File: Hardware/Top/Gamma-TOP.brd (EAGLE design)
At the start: 38 x 38 mm, 65 parts, among them SW1 SWITCH.MOM, SW2 SWITCH.MOM, U1 FT231XS, U3 NRF52832_MODULE_MDBT42, U4 PCF8523

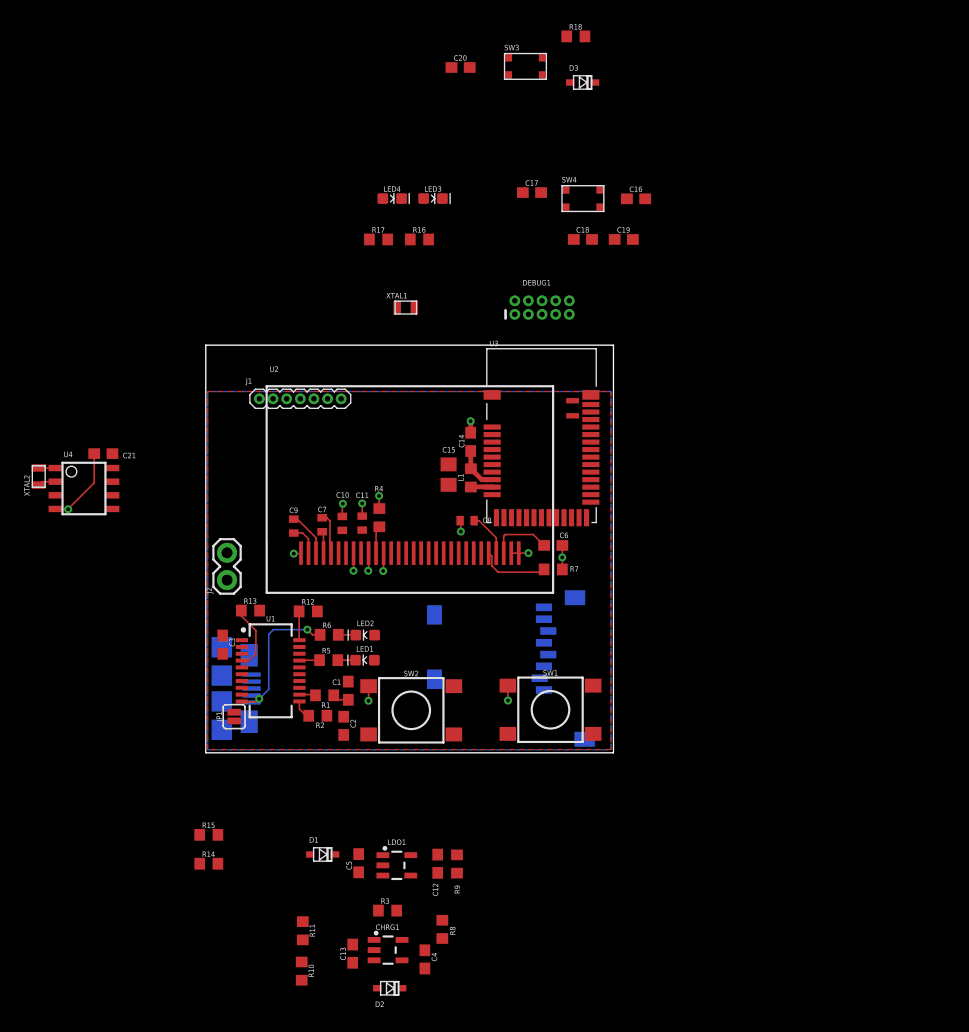
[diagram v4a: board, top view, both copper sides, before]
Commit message: This is the routing as of Take 006 before the removal of the SD Card
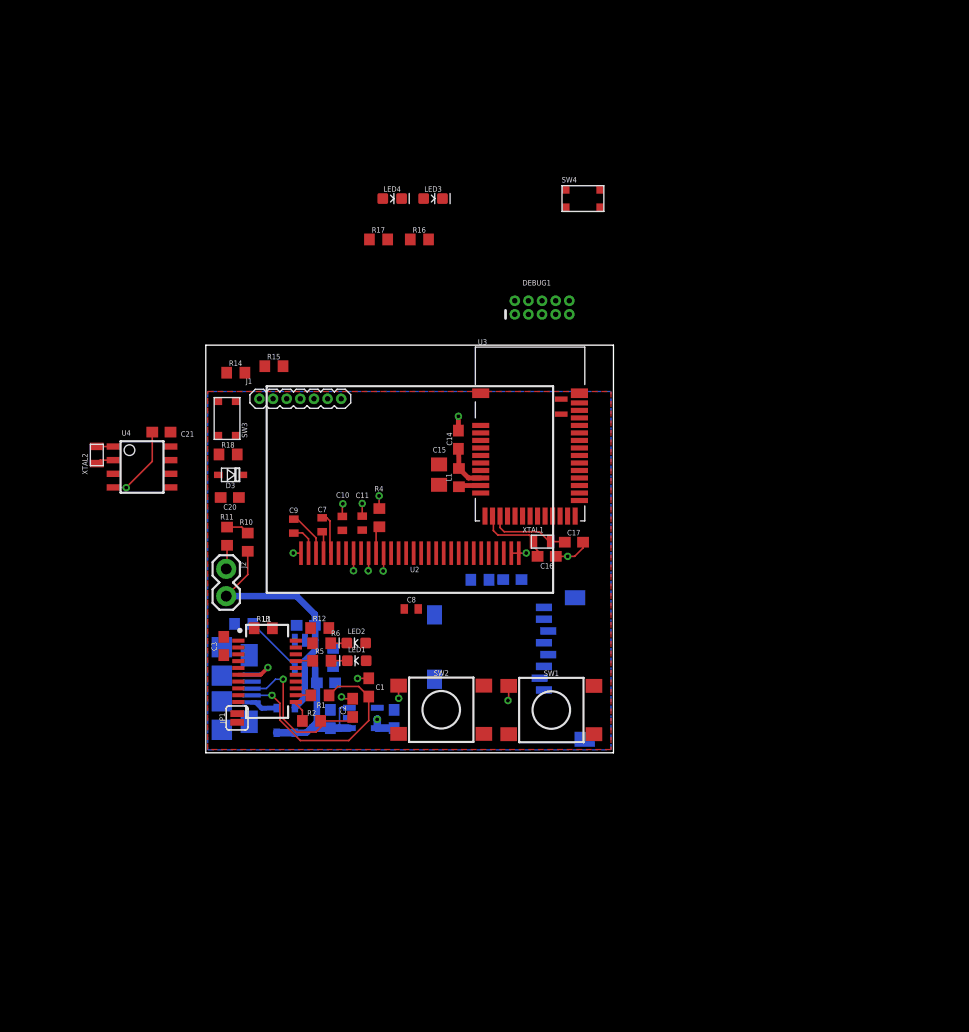
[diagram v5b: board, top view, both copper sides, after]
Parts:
- removed C18, C19: 300p, LinnesLab-Passives:C0603
- removed R9: 100k, LinnesLab-Passives:R0603
- moved R18 50.7 mm to (2.08, 27.8)
- moved D3 49.1 mm to (2.31, 25.9)
- moved R14 45.8 mm to (2.79, 35.4)
- moved C20 45.5 mm to (2.24, 23.8), turned to 180 degrees
- moved R15 44.1 mm to (6.35, 36.0)
- moved SW3 43.0 mm to (1.98, 31.2), turned to 90 degrees
- moved R10 40.3 mm to (3.91, 19.6)
- moved R11 37.5 mm to (1.98, 20.2), turned to 90 degrees
- moved C16 34.4 mm to (31.8, 18.3), turned to 180 degrees
- moved R8 34.0 mm to (3.53, 12.0), flipped to the bottom, turned to 180 degrees
- moved C17 32.8 mm to (34.3, 19.6)
- moved C13 30.9 mm to (9.32, 11.9), flipped to the bottom, turned to 0 degrees
- moved CHRG1 28.7 mm to (9.25, 9.19), flipped to the bottom, turned to 180 degrees
- moved C4 27.4 mm to (11.2, 6.53), flipped to the bottom, turned to 0 degrees
- moved D2 27.1 mm to (6.60, 3.02), flipped to the bottom, turned to 270 degrees
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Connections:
- net 3.3V: no longer R9.2
- net GND: no longer C18.2, C19.2, R9.1
- net P0.09/NFC1: no longer C18.1
- net P0.10/NFC2: no longer C19.1
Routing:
- net VLIPO: track 0.00 -> 23.5 mm
- net USB-: track 1.53 -> 21.0 mm, vias 0 -> 1
- net VIN: track 0.00 -> 15.6 mm
- net USB+: track 0.00 -> 14.9 mm, vias 0 -> 1
- net TXLED: track 13.3 -> 0.04 mm, vias 2 -> 0
- net N$6: track 0.00 -> 7.67 mm
- net GND: track 25.4 -> 32.9 mm, vias 14 -> 16
- net N$4: track 0.00 -> 7.22 mm
- net N$2: track 6.53 -> 0.00 mm
- net RXD.FT: track 6.15 -> 0.00 mm
- net N$13: track 5.83 -> 0.00 mm
- net N$17: track 0.00 -> 5.74 mm
- net N$15: track 4.16 -> 0.27 mm
- net TXD.FT: track 2.69 -> 0.03 mm
- net V_USB: track 0.00 -> 2.55 mm
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
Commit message: Partway through Take 007
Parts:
- removed C21: 1u, LinnesLab-Passives:C0603
- removed SD1: (no value), LinnesLab-Connectors:MICROSD
- removed U4: PCF8523, LinnesLab-Clocks:SO8
- removed XTAL1: 32.768kHz, LinnesLab-Clocks:2-SMD.NOLEAD.2.0MMTO1.2MM
- removed XTAL2: 32.7680kHz, LinnesLab-Clocks:2-SMD.NOLEAD.2.0MMTO1.2MM
- added Y1: 32.768kHz, LinnesLab-Clocks:2-SMD.NOLEAD.2.0MMTO1.2MM
- C8: device LinnesLab-Passives:C0402 -> LinnesLab-Passives:C0603
- LED2: value YELLOW -> BLUE
- LED4: value BLUE -> YELLOW
- moved LED3 43.7 mm to (14.1, 8.59), turned to 180 degrees
- moved LED4 41.6 mm to (14.0, 10.2), turned to 180 degrees
- moved R18 36.9 mm to (35.8, 12.8), turned to 180 degrees
- moved SW3 36.9 mm to (35.5, 15.8)
- moved D3 36.6 mm to (35.7, 10.8), turned to 180 degrees
- moved C20 36.5 mm to (35.7, 9.12), turned to 0 degrees
- moved R17 31.2 mm to (35.9, 23.7), turned to 90 degrees
- moved R16 28.1 mm to (34.4, 23.7), turned to 90 degrees
- moved LED2 24.2 mm to (35.9, 20.7), turned to 270 degrees
- moved LED1 23.7 mm to (34.5, 20.6), turned to 270 degrees
- moved SW4 15.8 mm to (35.6, 35.9), turned to 180 degrees
- moved C17 15.7 mm to (18.9, 22.5), turned to 90 degrees
- moved C16 14.9 mm to (17.5, 22.5), turned to 270 degrees
- moved DEBUG1 12.9 mm to (35.7, 29.4), turned to 270 degrees
- moved C8 11.1 mm to (30.2, 14.1), turned to 180 degrees
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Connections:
- removed net CD2: SD1.CD2
- removed net N$19: U4.2, XTAL2.P$1
- removed net N$20: U4.1, XTAL2.P$2
- removed net VBATT: U4.3
- net 3.3V: now also LED3.A, LED4.A; no longer C21.1, LED1.A, LED2.A, SD1.4, U4.8
- net D5/CD1: no longer SD1.CD1
- net D7/SD.CS: no longer SD1.2
- net GND: now also LED1.C, LED2.C; no longer C21.2, LED3.C, LED4.C, SD1.6, SD1.MT1, SD1.MT2, U4.4
- net MISO: no longer SD1.7
- net MOSI: no longer SD1.3
- net N$10: now also LED2.A; no longer LED4.A
- net N$25: now also LED3.C; no longer LED1.C
- net N$26: now also LED4.C; no longer LED2.C
- net N$4: now also Y1.P$1; no longer XTAL1.P$1
- net N$6: now also Y1.P$2; no longer XTAL1.P$2
- net N$9: now also LED1.A; no longer LED3.A
- net SCK: no longer SD1.5
- net SCL: no longer U4.6
- net SDA: no longer U4.5
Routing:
- net RESET: track 0.00 -> 30.7 mm, vias 0 -> 1
- net D15/SW2: track 0.00 -> 24.3 mm, vias 0 -> 2
- net D11/SW1: track 0.00 -> 20.6 mm
- net MOSI: track 0.00 -> 19.5 mm, vias 0 -> 2
- net D16/CS.OLED: track 0.00 -> 18.9 mm, vias 0 -> 1
- net SCK: track 0.00 -> 15.6 mm, vias 0 -> 2
- net D3/RESET.OLED: track 0.00 -> 12.2 mm, vias 0 -> 2
- net D4/DC.OLED: track 0.00 -> 11.7 mm, vias 0 -> 2
- net SWO: track 0.00 -> 11.3 mm, vias 0 -> 1
- net DFU: track 0.00 -> 11.2 mm, vias 0 -> 2
- net SWCLK: track 0.00 -> 9.31 mm
- net LED2: track 0.00 -> 7.69 mm
- net N$2: track 0.00 -> 7.46 mm
- net N$15: track 0.27 -> 6.34 mm
- net SWDIO: track 0.00 -> 5.43 mm, vias 0 -> 1
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
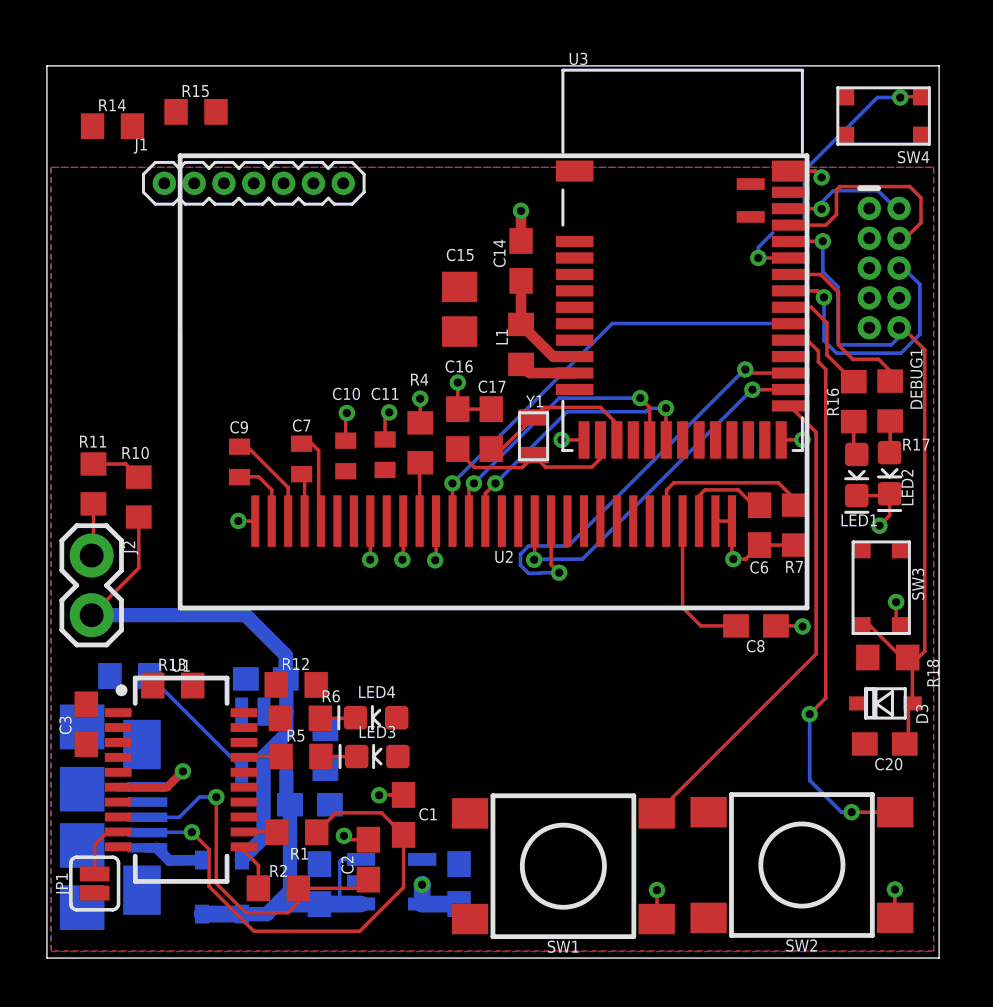
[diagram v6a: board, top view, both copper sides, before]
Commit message: Take 007 35:16, before I attempt to move the power circuit on bottom of Top board out to the outside regions
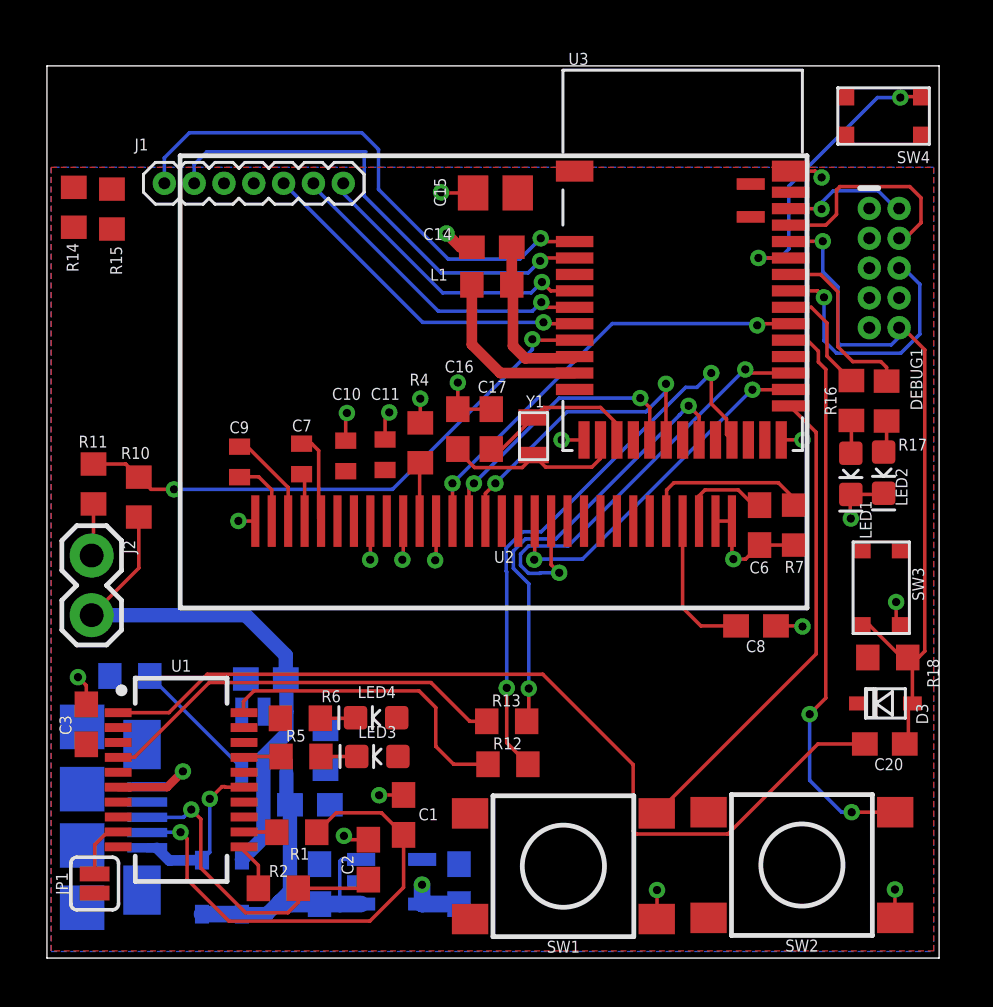
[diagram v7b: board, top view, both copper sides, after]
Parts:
- moved R13 14.3 mm to (19.6, 10.1)
- moved R12 9.63 mm to (19.6, 8.26)
- moved R15 5.47 mm to (2.77, 31.9), turned to 90 degrees
- moved C15 5.18 mm to (19.1, 32.6), turned to 0 degrees
- moved R14 3.83 mm to (1.14, 32.0), turned to 90 degrees
- moved L1 2.83 mm to (18.9, 28.7), turned to 0 degrees
- moved C14 1.37 mm to (18.9, 30.3), turned to 180 degrees
- moved LED1 0.26 mm to (34.2, 20.6)
- moved LED2 0.26 mm to (35.6, 20.7)
- moved R17 0.15 mm to (35.8, 23.7)
- moved R16 0.11 mm to (34.3, 23.7)
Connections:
- removed net A4/BATT: R10.1, R11.2, U3.5
- removed net A6/TIA: J1.6, U3.7
- removed net A7/PPG: J1.7, U3.8
- removed net D29/LED.CTRL: J1.5, U3.6
- new net A4/PPG: J1.7, U3.5
- new net A5/TIA: J1.6, U3.6
- new net A7/BATT: R10.1, R11.2, U3.8
- new net D30/LED.CTRL: J1.5, U3.7
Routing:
- net DTR: track 0.00 -> 38.5 mm
- net RXD.NRF: track 0.00 -> 24.6 mm, vias 0 -> 2
- net A7/BATT: track 0.00 -> 23.9 mm, vias 0 -> 2
- net SDA: track 0.00 -> 22.7 mm, vias 0 -> 1
- net SCL: track 0.00 -> 20.8 mm, vias 0 -> 1
- net TXD.NRF: track 0.00 -> 19.2 mm, vias 0 -> 2
- net RXD.FT: track 0.00 -> 17.7 mm
- net D30/LED.CTRL: track 0.00 -> 14.9 mm, vias 0 -> 1
- net A5/TIA: track 0.00 -> 13.7 mm, vias 0 -> 1
- net TXD.FT: track 0.03 -> 13.4 mm
- net A4/PPG: track 0.00 -> 12.4 mm, vias 0 -> 1
- net N$11: track 2.44 -> 7.43 mm
- net V_USB: track 2.55 -> 6.99 mm, vias 0 -> 1
- net GND: track 36.8 -> 39.0 mm, vias 21 -> 23
- net A4/BATT: track 2.16 -> 0.00 mm
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
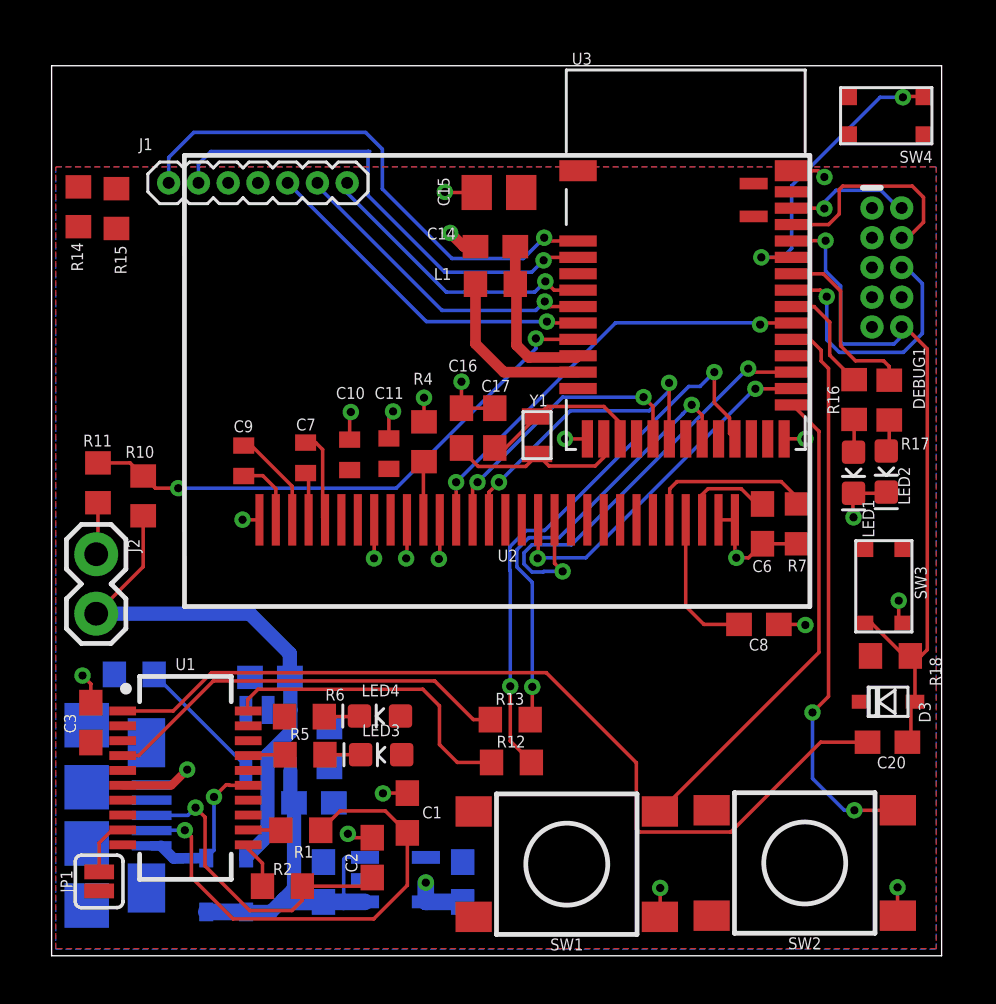
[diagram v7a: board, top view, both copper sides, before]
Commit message: Finished with Preliminary Version A of Smartwatch as of end of Take 008 video
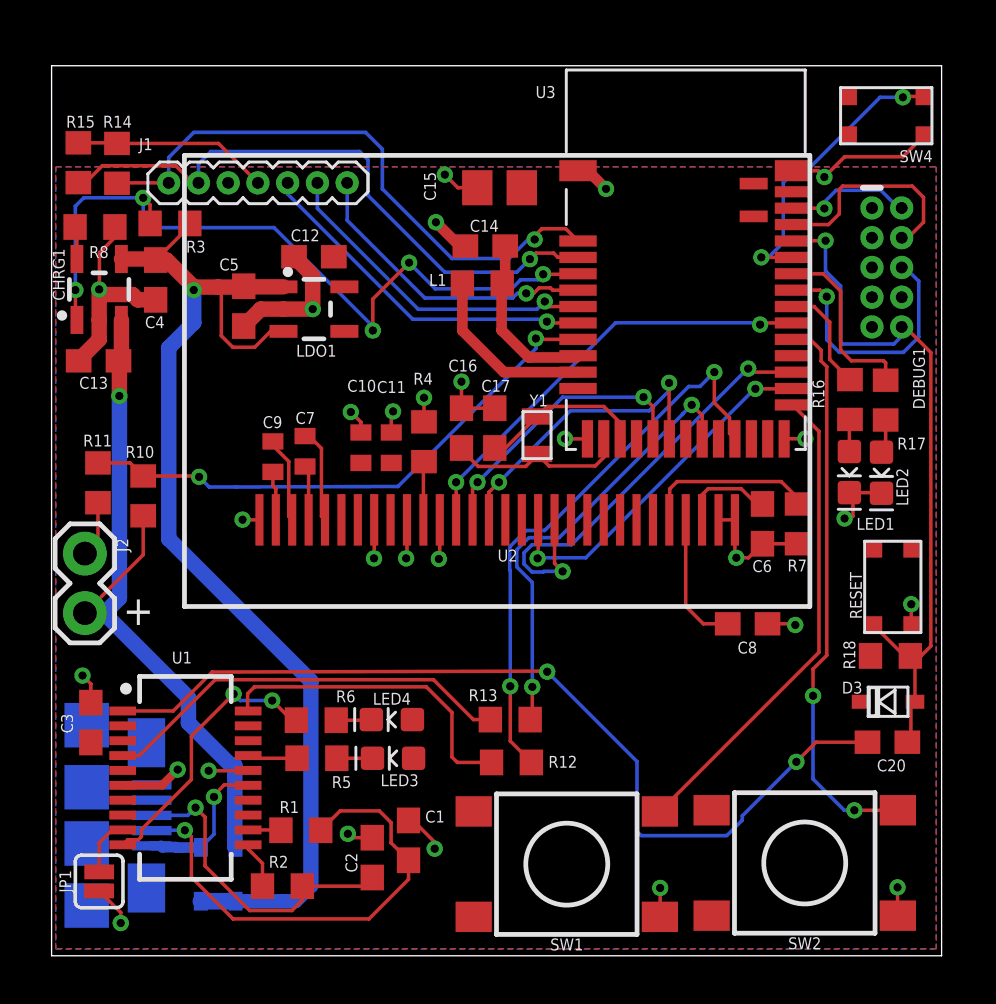
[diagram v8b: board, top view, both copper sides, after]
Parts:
- removed SW3: (no value), LinnesLab-Switches:BUTTON-GULLWING
- added RESET: (no value), LinnesLab-Switches:BUTTON-GULLWING
- R8: value (none) -> 5k
- moved C12 27.4 mm to (11.2, 29.8), flipped to the top, turned to 180 degrees
- moved C5 24.8 mm to (8.20, 27.7), flipped to the top, turned to 90 degrees
- moved LDO1 24.6 mm to (11.2, 27.6), flipped to the top, turned to 270 degrees
- moved R3 23.4 mm to (5.05, 31.3), flipped to the top, turned to 0 degrees
- moved C4 23.3 mm to (4.45, 28.9), flipped to the top, turned to 90 degrees
- moved CHRG1 20.6 mm to (2.03, 28.4), flipped to the top, turned to 0 degrees
- moved R8 19.2 mm to (1.85, 31.1), flipped to the top
- moved C13 15.4 mm to (2.01, 25.4), flipped to the top, turned to 180 degrees
- moved R15 2.54 mm to (1.14, 33.9), turned to 270 degrees
- moved R14 2.48 mm to (2.79, 33.8), turned to 270 degrees
- moved C9 1.26 mm to (9.45, 21.3)
- moved C1 1.17 mm to (15.2, 4.93)
- moved D1 0.65 mm to (7.85, 3.48)
- moved C10 0.57 mm to (13.2, 21.7)
- moved L1 0.56 mm to (18.4, 28.7)
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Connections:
- net GND: now also RESET.3; no longer SW3.3
- net RESET: now also RESET.1; no longer SW3.1
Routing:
- net D27/CHRG.STATUS: track 0.00 -> 33.5 mm, vias 0 -> 5
- net VIN: track 15.6 -> 48.4 mm, vias 0 -> 1
- net GND: track 39.0 -> 64.6 mm, vias 23 -> 28
- net TXLED: track 0.04 -> 11.8 mm, vias 0 -> 2
- net VLIPO: track 23.5 -> 32.1 mm, vias 0 -> 1
- net 3.3V: track 2.40 -> 8.37 mm, vias 1 -> 0
- net SCL: track 20.8 -> 26.4 mm
- net N$17: track 5.74 -> 1.40 mm
- net SDA: track 22.7 -> 25.3 mm
- net N$3: track 2.94 -> 2.10 mm
- net V_USB: track 6.99 -> 6.25 mm
- net A4/PPG: track 12.4 -> 13.1 mm
- net RXLED: track 1.59 -> 2.13 mm
- net N$5: track 4.22 -> 3.69 mm
- net A5/TIA: track 13.7 -> 14.2 mm
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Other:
- board text added: "+"
